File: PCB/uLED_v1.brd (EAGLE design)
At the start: 23.6 x 23.6 mm, 19 parts, among them IC2 ATSAMD21E18A-AFT, U1 AP2112K-3.3

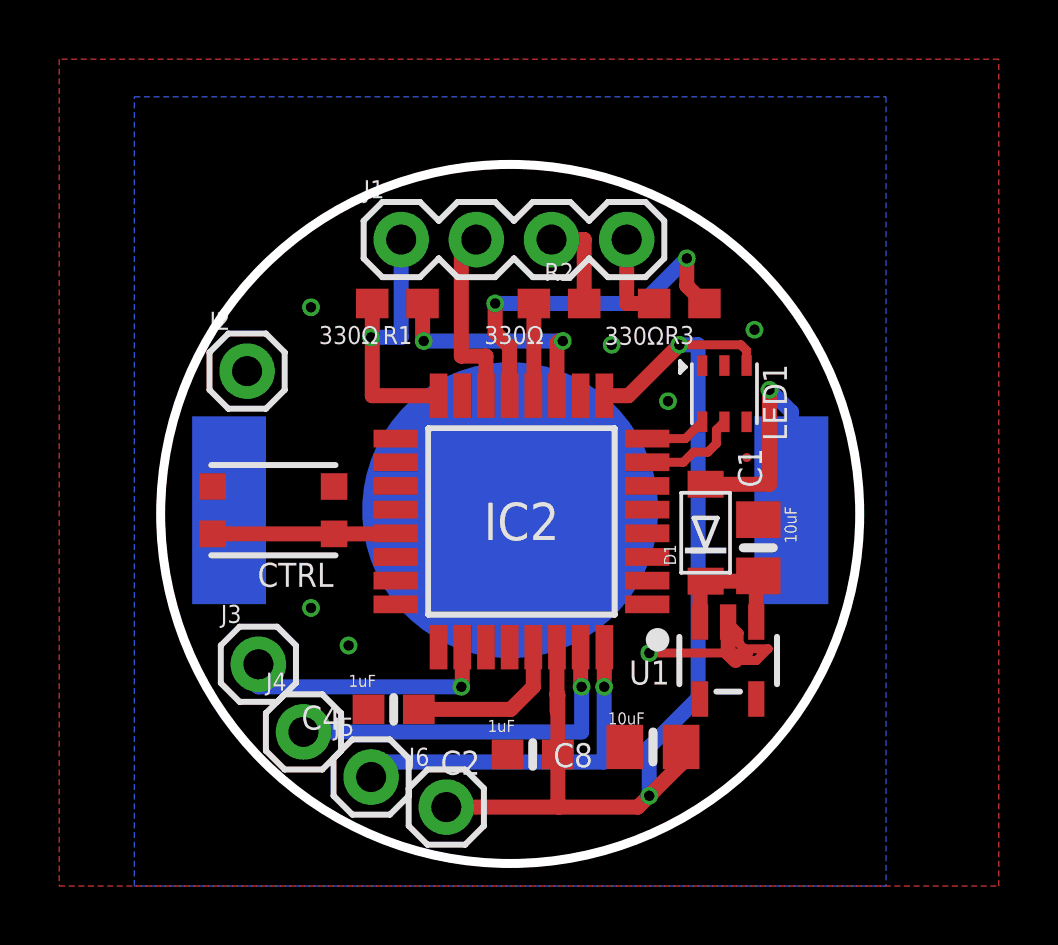
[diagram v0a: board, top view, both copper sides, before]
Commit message: Adding ADC to anotherDotstar
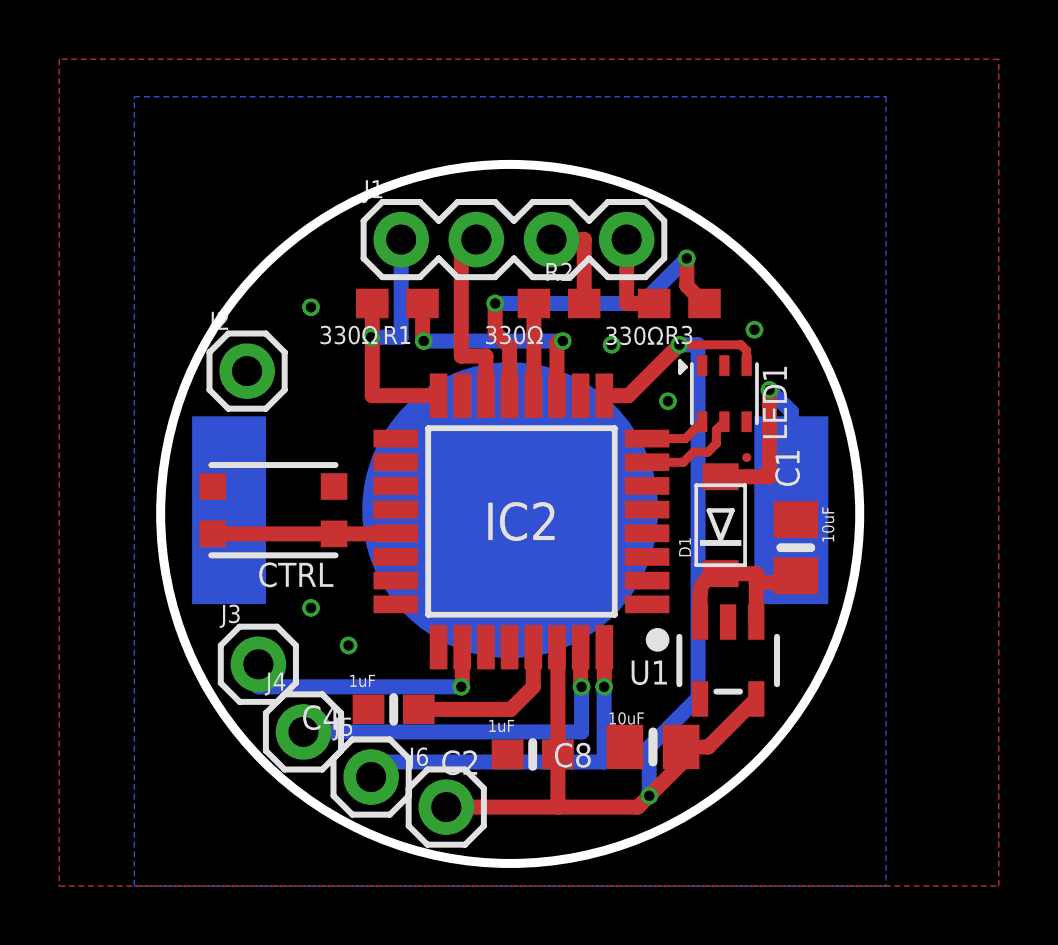
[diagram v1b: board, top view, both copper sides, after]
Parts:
- moved C1 1.27 mm to (57.9, 22.9)
- moved D1 0.57 mm to (55.4, 23.6)
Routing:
- net GND: track 8.17 -> 0.01 mm, vias 7 -> 6
- net 3.3V: track 37.8 -> 40.4 mm
- net VBAT: track 9.72 -> 8.95 mm
